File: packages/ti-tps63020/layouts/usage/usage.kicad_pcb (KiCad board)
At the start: 2 copper layers, 24 parts

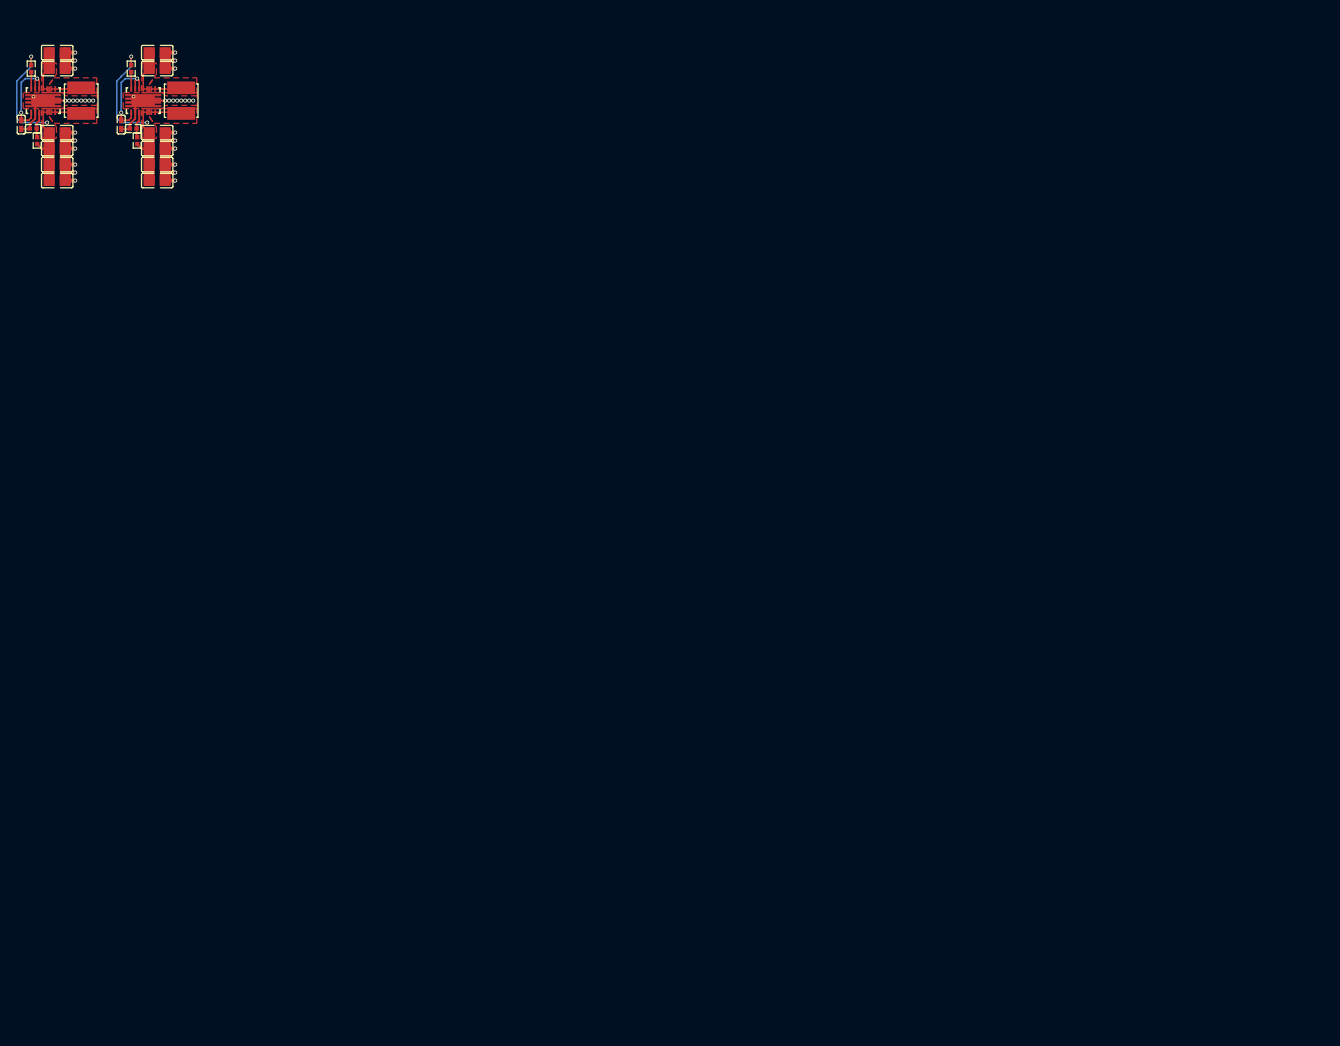
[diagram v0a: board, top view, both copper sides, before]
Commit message: fixing up tps564201
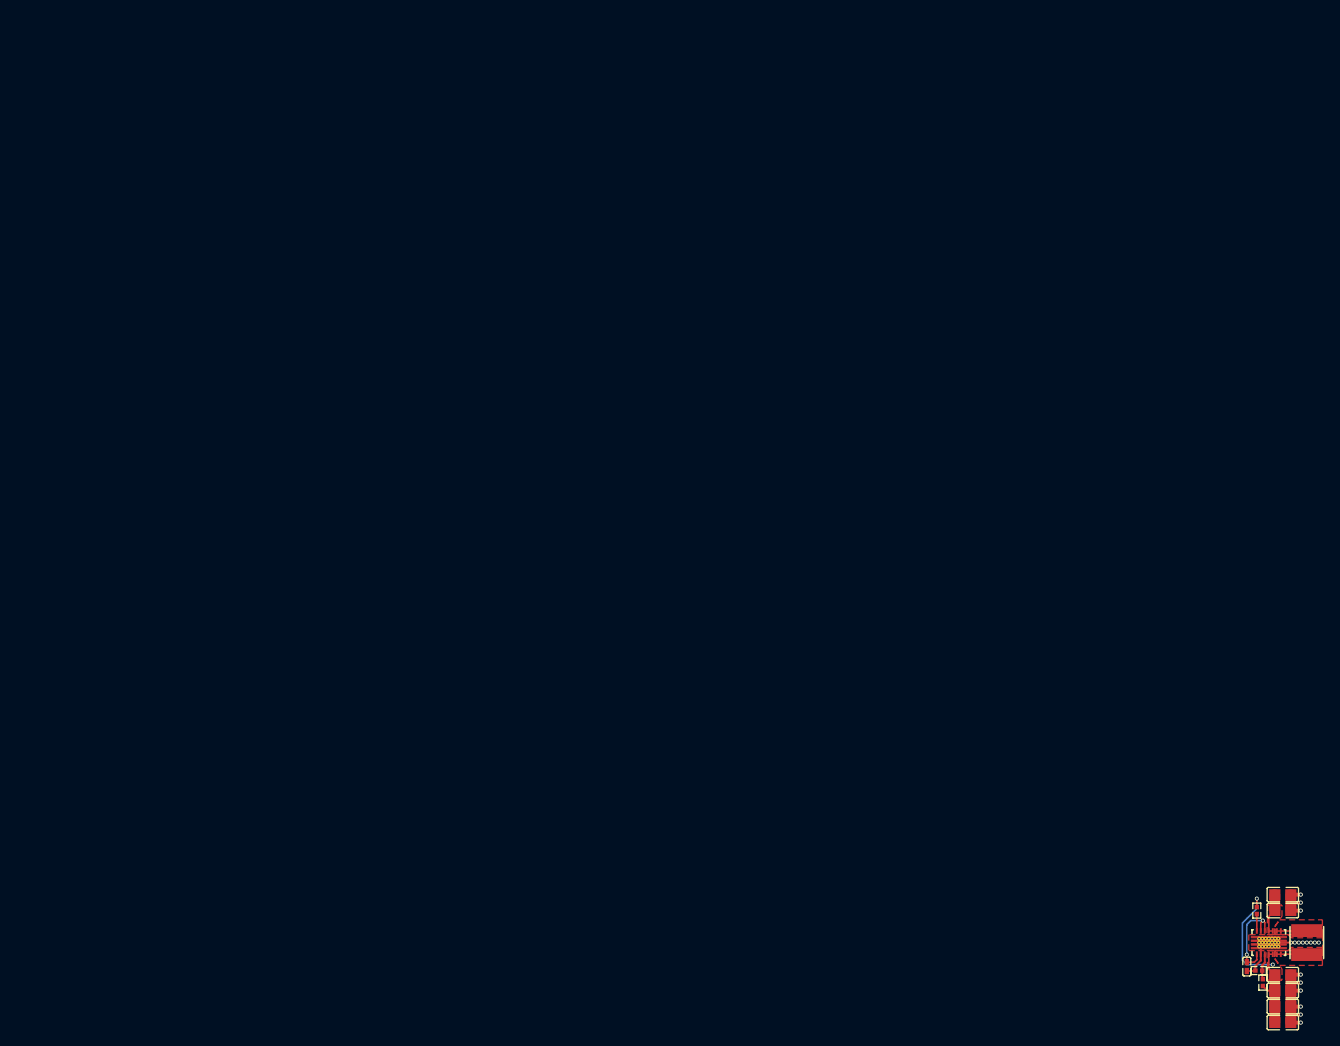
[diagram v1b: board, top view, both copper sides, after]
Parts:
- removed C10, C11, C12, C13: 22µF ±20% 25V X5R, Samsung_Electro_Mechanics_CL21A226MAQNNNE:C0805
- removed C14: 100nF ±10% 16V X7R, Samsung_Electro_Mechanics_CL05B104KO5NNNC:C0402
- removed C8, C9: 10µF ±10% 25V X5R, Samsung_Electro_Mechanics_CL21A106KAYNNNE:C0805
- removed L2: 1µH ±20% 6.7A 23mΩ, cjiang_FHD4020S_1R0MT:IND-SMD_L4.0-W4.0
- removed R4: 200kΩ ±1% 62.5mW, UNI_ROYAL_0402WGF2003TCE:R0402
- removed R5: 1.2MΩ ±1% 62.5mW, UNI_ROYAL_0402WGF1204TCE:R0402
- removed R6: 1MΩ ±1% 62.5mW, UNI_ROYAL_0402WGF1004TCE:R0402
- removed U2: , Texas_Instruments_TPS63020DSJR:VSON-14_L4.0-W3.0-P0.50-BL-EP_TI_DSJ
- C3, C4, C5, C6: value 22µF ±20% 25V X5R -> 22µF ±20% 6.3V X5R; footprint Samsung_Electro_Mechanics_CL21A226MAQNNNE:C0805 -> Samsung_Electro_Mechanics_CL21A226MQQNNNE:C0805
- L1: value 1µH ±20% 6.7A 23mΩ -> 1µH ±20% 4.7A 18mΩ; footprint cjiang_FHD4020S_1R0MT:IND-SMD_L4.0-W4.0 -> cjiang_FNR4030S1R0MT:IND-SMD_L4.0-W4.0_FNR40XXS
- R1: value 150kΩ ±1% 62.5mW -> 180kΩ ±1% 62.5mW; footprint UNI_ROYAL_0402WGF1503TCE:R0402 -> YAGEO_RC0402FR_07180KL:R0402
- R2: value 510kΩ ±1% 62.5mW -> 1MΩ ±1% 62.5mW; footprint UNI_ROYAL_0402WGF5103TCE:R0402 -> UNI_ROYAL_0402WGF1004TCE:R0402
- moved C1 185.9 mm to (154.9, 101.2)
- moved C2 185.9 mm to (154.9, 99.2)
- moved C3 185.9 mm to (154.9, 115.2)
- moved C4 185.9 mm to (154.9, 113.2)
- moved C5 185.9 mm to (154.9, 111.2)
- moved C6 185.9 mm to (154.9, 109.2)
- moved C7 185.9 mm to (150.4, 108.2)
- moved L1 185.9 mm to (157.9, 105.2)
- moved R1 185.9 mm to (151.9, 108.8)
- moved R2 185.9 mm to (152.4, 110.2)
- moved R3 185.9 mm to (151.7, 101.2)
- moved U1 185.9 mm to (153.2, 105.2)
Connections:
- net -VOUT-0 renamed power-VCC
- net VIN renamed power_in-VCC
- net gnd renamed GND
- net regulator_1v8-EN renamed _power_in_a-VCC
- net regulator_1v8-FB renamed VDIV_OUTPUT
- net regulator_1v8-L1 renamed L1
- net regulator_1v8-L2 renamed L2
- net regulator_1v8-PG renamed PG
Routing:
- net GND: track 62.7 -> 31.4 mm, vias 34 -> 17
- net -VOUT-1: track 24.6 -> 0.00 mm, vias 2 -> 0
- net regulator_3v3-EN: track 11.8 -> 0.00 mm, vias 2 -> 0
- net power_in-VCC: track 10.7 -> 5.36 mm
- net regulator_3v3-L2: track 3.81 -> 0.00 mm
- net regulator_3v3-L1: track 3.81 -> 0.00 mm
- net regulator_3v3-FB: track 3.28 -> 0.00 mm
- net regulator_3v3-PG: track 2.12 -> 0.00 mm
- removed copper zone on F.Cu, net -VOUT-1
- removed copper zone on F.Cu, net regulator_3v3-L1
- removed copper zone on F.Cu, net regulator_3v3-L2

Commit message: fix ti-tps63020
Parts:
- C1, C2: value 10µF ±10% 25V X5R -> 9.999999999999999e-06F
- C3, C4, C5, C6: value 22µF ±20% 6.3V X5R -> 2.2e-05F
- C7: value 100nF ±10% 16V X7R -> 1.0000000000000001e-07F
- L1: value 1µH ±20% 4.7A 18mΩ -> L 1e-06H
- R1: value 180kΩ ±1% 62.5mW -> 150000.0Ω
- R2: value 1MΩ ±1% 62.5mW -> 10000.0Ω
- R3: value 1MΩ ±1% 62.5mW -> 1000000.0Ω
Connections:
- net GND renamed lv
- net L1 renamed 8
- net L2 renamed 6
- net _power_in_a-VCC renamed power_in_a_capacitor-power-hv
- net power-VCC renamed output_decoupling_capacitor[3]-power-hv
- net power_in-VCC renamed input_decoupling_capacitor[1]-power-hv

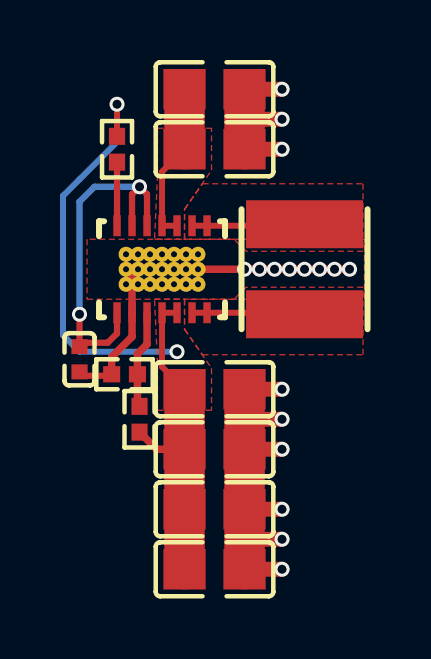
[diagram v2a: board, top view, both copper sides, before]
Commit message: remove all those other changes, just bosch baby
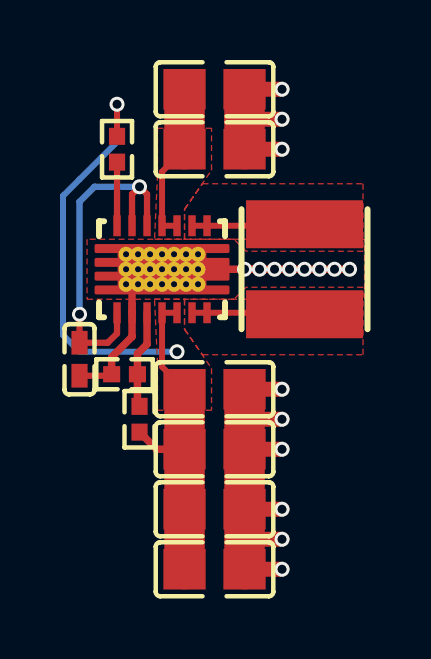
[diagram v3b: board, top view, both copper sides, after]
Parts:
- C1, C2: value 9.999999999999999e-06F -> 10µF ±10% 25V X5R
- C3, C4, C5, C6: value 2.2e-05F -> 22µF ±20% 6.3V X5R
- C7: value 1.0000000000000001e-07F -> 100nF ±10% 16V X7R
- L1: value L 1e-06H -> 1µH ±20% 4.7A 18mΩ
- R1: value 150000.0Ω -> 180kΩ ±1% 62.5mW
- R2: value 10000.0Ω -> 1MΩ ±1% 62.5mW
- R3: value 1000000.0Ω -> 1MΩ ±1% 62.5mW
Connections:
- net 6 renamed L2
- net 8 renamed L1
- net input_decoupling_capacitor[1]-power-hv renamed power_in-VCC
- net lv renamed GND
- net output_decoupling_capacitor[3]-power-hv renamed power-VCC
- net power_in_a_capacitor-power-hv renamed _power_in_a-VCC

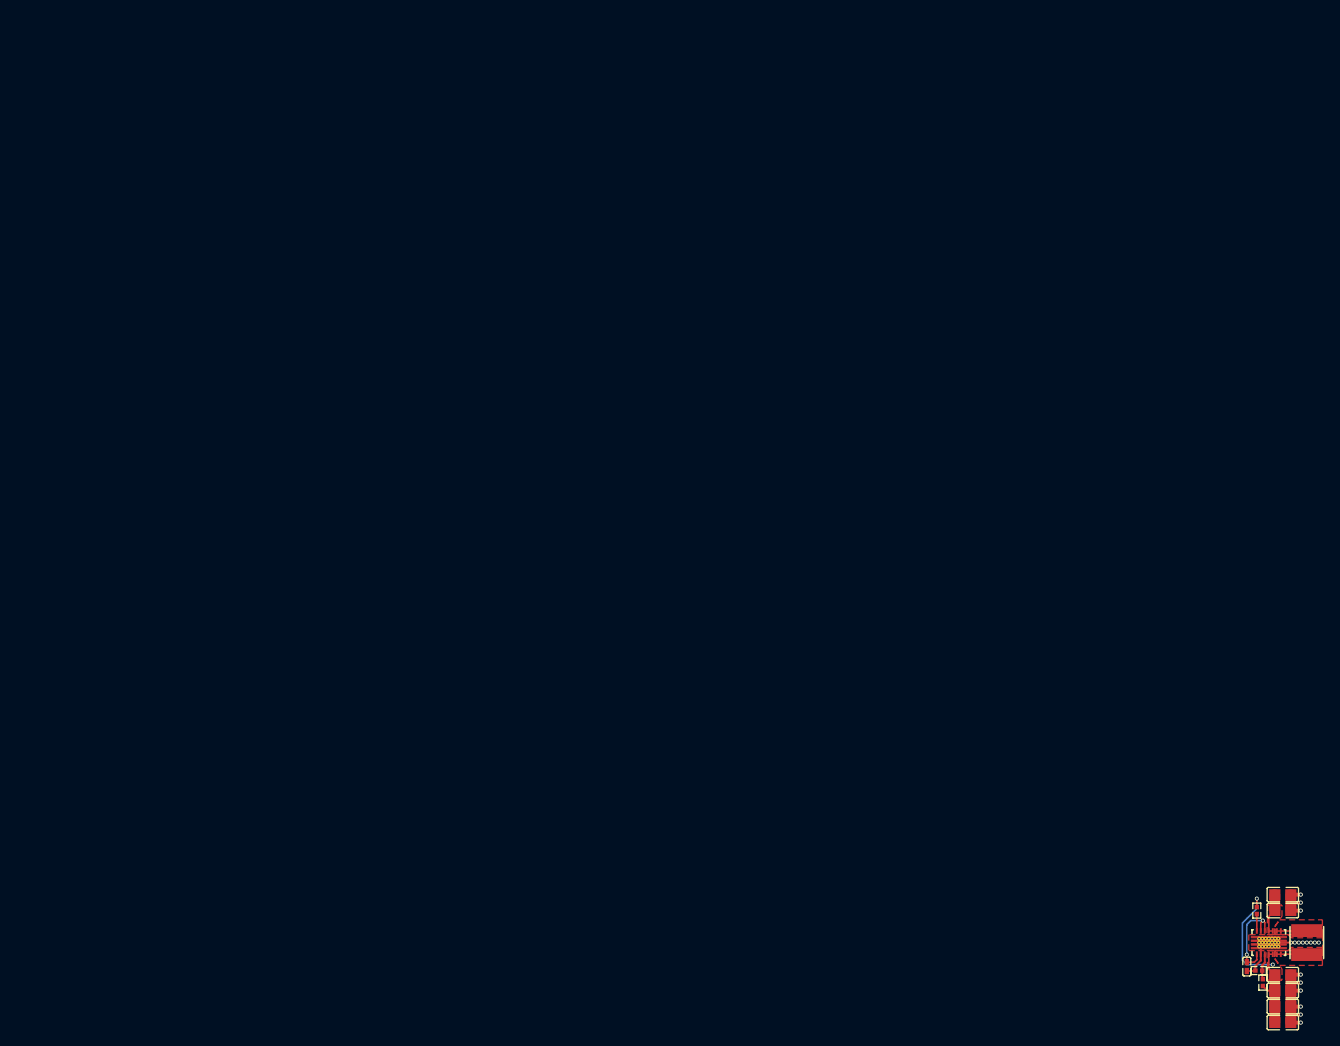
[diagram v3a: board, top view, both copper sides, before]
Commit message: ti-tps63020: package update to v0.3.0, ato:^0.14.0 (#306)
* ti-tps63020: package update to v0.3.0, ato:^0.14.0

Build targets:
  default = rc0
  usage = rc0
Package Verify: rc0
Version: 0.2.3 -> 0.3.0
Requires ato: ^0.14.0

* Update main.yml from main

Syncs GitHub Actions workflow configuration.

* ci: update workflow from main (fix package publish git issue)

* stuck in solver loop

* remove R0402

* build success

* remove broken parts

* add previously broken parts

* remove stale import

---------

Co-authored-by: Nicholas Krstevski <nick@atopile.io>
Co-authored-by: Nick Krstevski <51719418+nickkrstevski@users.noreply.github.com>
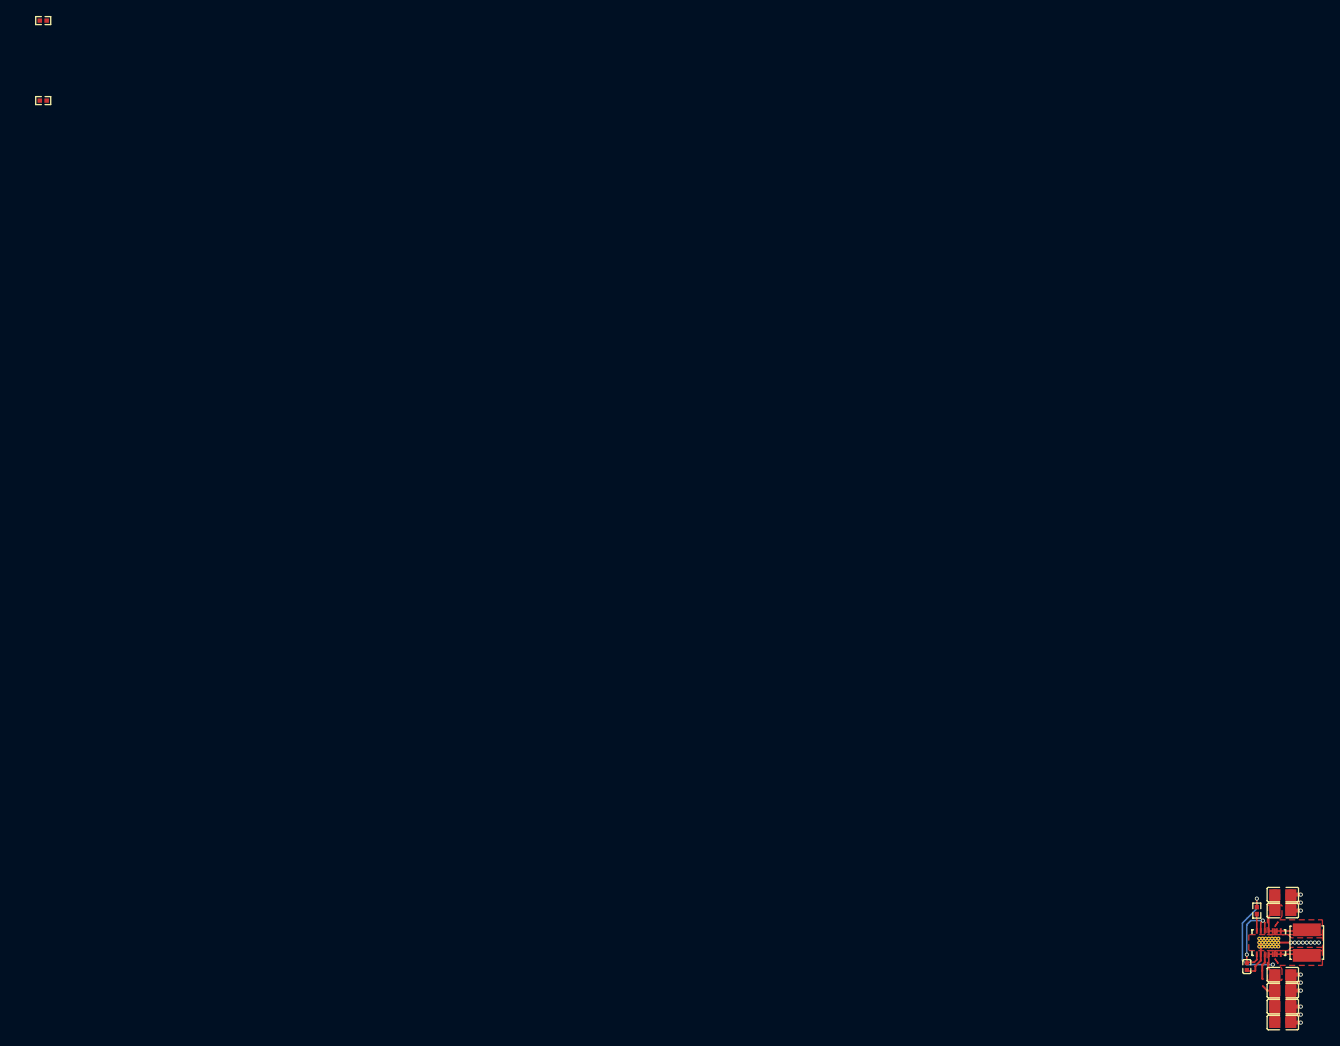
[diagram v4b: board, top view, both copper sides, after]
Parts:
- C1, C2: value 10µF ±10% 25V X5R -> 0F
- C3, C4, C5, C6: value 22µF ±20% 6.3V X5R -> 0F; footprint Samsung_Electro_Mechanics_CL21A226MQQNNNE:C0805 -> Samsung_Electro_Mechanics_CL21A226MAQNNNE:C0805
- C7: value 100nF ±10% 16V X7R -> 0F
- L1: value 1µH ±20% 4.7A 18mΩ -> L 0H; footprint cjiang_FNR4030S1R0MT:IND-SMD_L4.0-W4.0_FNR40XXS -> cjiang_FHD4020S_1R0MT:IND-SMD_L4.0-W4.0
- R1: value 180kΩ ±1% 62.5mW -> 150000Ω; footprint YAGEO_RC0402FR_07180KL:R0402 -> FOJAN_FRC0402F1503TS:R0402
- R2: value 1MΩ ±1% 62.5mW -> 22000Ω; footprint UNI_ROYAL_0402WGF1004TCE:R0402 -> UNI_ROYAL_0402WGF2202TCE:R0402
- R3: value 1MΩ ±1% 62.5mW -> 1000000Ω
- moved R1 192.8 mm to (0.00, -10.0), turned to 0 degrees
- moved R2 188.1 mm to (0.00, 0.00), turned to 0 degrees
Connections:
- net L1 renamed 8
- net L2 renamed 6
- net _power_in_a-VCC renamed hv
- net power_in-VCC renamed input_decoupling_capacitor[1]-power-hv
- C1 pad 2: GND -> input_decoupling_capacitor[1]-power-lv
- C2 pad 2: GND -> input_decoupling_capacitor[1]-power-lv
- C3 pad 1: power-VCC -> output_decoupling_capacitor[3]-power-hv
- C3 pad 2: GND -> output_decoupling_capacitor[3]-power-lv
- C4 pad 1: power-VCC -> output_decoupling_capacitor[3]-power-hv
- C4 pad 2: GND -> output_decoupling_capacitor[3]-power-lv
- C5 pad 1: power-VCC -> output_decoupling_capacitor[3]-power-hv
- C5 pad 2: GND -> output_decoupling_capacitor[3]-power-lv
- C6 pad 1: power-VCC -> output_decoupling_capacitor[3]-power-hv
- C6 pad 2: GND -> output_decoupling_capacitor[3]-power-lv
- C7 pad 2: GND -> lv
- R1 pad 1: VDIV_OUTPUT -> output_decoupling_capacitor[3]-power-hv
- R1 pad 2: GND -> ref_out-hv
- R2 pad 1: power-VCC -> ref_out-hv
- R2 pad 2: VDIV_OUTPUT -> output_decoupling_capacitor[3]-power-lv
- R3 pad 2: power-VCC -> output_decoupling_capacitor[3]-power-hv
- U1 pad 15: GND -> input_decoupling_capacitor[1]-power-lv
- U1 pad 2: GND -> input_decoupling_capacitor[1]-power-lv
- U1 pad 3: VDIV_OUTPUT -> ref_out-hv
- U1 pad 4: power-VCC -> output_decoupling_capacitor[3]-power-hv
- U1 pad 5: power-VCC -> output_decoupling_capacitor[3]-power-hv
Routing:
- net input_decoupling_capacitor[1]-power-lv: track 0.00 -> 31.4 mm, vias 0 -> 17
- net GND: track 31.4 -> 0.00 mm, vias 17 -> 0
- net power-VCC: track 24.6 -> 0.00 mm, vias 2 -> 0
- net output_decoupling_capacitor[3]-power-hv: track 0.00 -> 24.6 mm, vias 0 -> 2
- net 8: track 3.81 -> 0.00 mm
- net 3: track 0.00 -> 3.81 mm
- net 6: track 3.81 -> 7.09 mm
- net VDIV_OUTPUT: track 3.28 -> 0.00 mm
- added copper zone on F.Cu, net input_decoupling_capacitor[1]-power-lv
- added copper zone on F.Cu, net output_decoupling_capacitor[3]-power-hv
- removed copper zone on F.Cu, net GND
- removed copper zone on F.Cu, net power-VCC
